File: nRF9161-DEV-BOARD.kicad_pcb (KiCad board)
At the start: 4 copper layers, 50 x 37.5 mm, 84 parts, among them J2 U.FL_LTE_NR+, J20 HOST_1x10_2.54, J5 U.FL_GNSS, J7 nanoSIM_4FF, J8 SWD_10pin, Q1 BSS138, SW2 RESET, U1 NRF9161-LACA-R7, U2 TLV73333PDBV, U3 TPS22919DCKR, U4 TPD3F303DPV, U5 SN74LXC2T45, U6 SN74LXC2T45, U7 SN74LXC1T45, U8 SN74LXC1T45

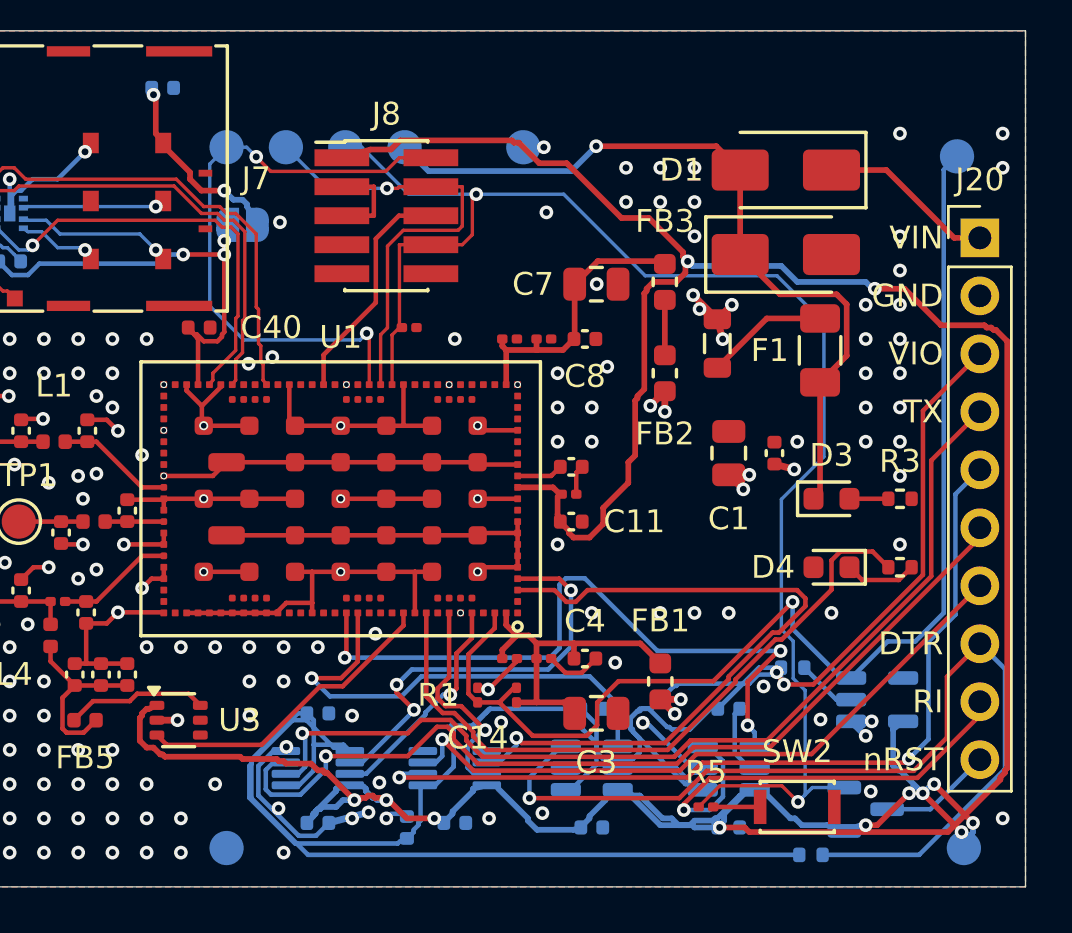
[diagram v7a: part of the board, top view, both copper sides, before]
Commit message: v2b-2: VDD_GPIO re-routed at 0.3 mm POWER clearance (141 mm vs 148 mm, 16 vias)
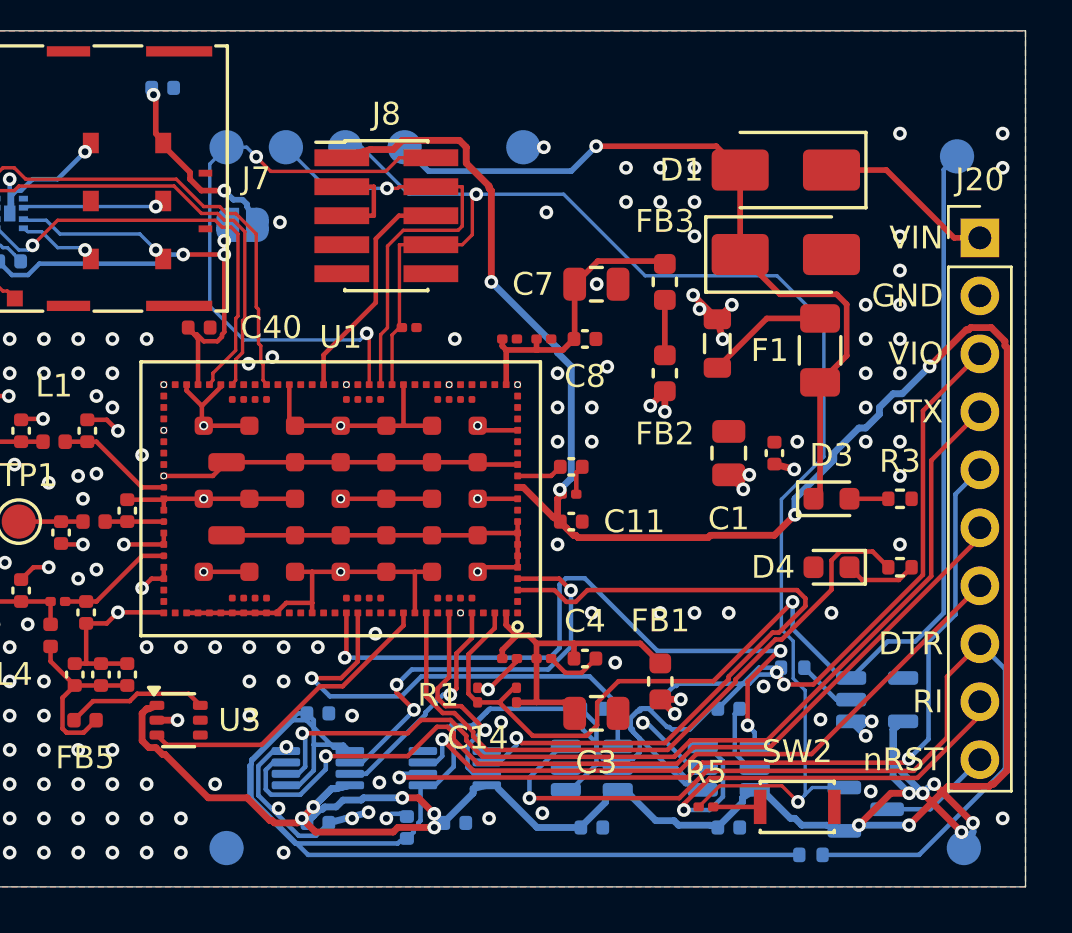
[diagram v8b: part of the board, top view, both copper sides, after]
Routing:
- net VDD_GPIO: track 147.7 -> 141.4 mm, vias 12 -> 16
